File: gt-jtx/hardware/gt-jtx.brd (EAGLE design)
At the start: 100 x 80 mm, 8 parts, among them IC1 MEGA8-P

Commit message: Added ISCP pads on board for ATmega8 programming. Increased Route width for better transfer of toner to PCB. Routes are now on bottom layer so no need to mirror image for printing
git-svn-id: https://gt-jtx.googlecode.com/svn/trunk@18 79910f2a-facc-22ab-b1ea-80da55196309
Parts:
- added R2: (no value), resistor:0204V
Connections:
- new net N$25: IC1.1, R2.2
- net +5V: now also R2.1
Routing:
- net +5V: track 136.9 -> 153.7 mm, vias 0 -> 1
- net N$25: track 0.00 -> 6.35 mm, vias 0 -> 1
- net N$14: vias 0 -> 1
- net N$13: vias 0 -> 1
- net N$12: vias 0 -> 1
- net GND: vias 0 -> 1

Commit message: changed layer to use top layer.
git-svn-id: https://gt-jtx.googlecode.com/svn/trunk@19 79910f2a-facc-22ab-b1ea-80da55196309
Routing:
- net N$6: vias 0 -> 1

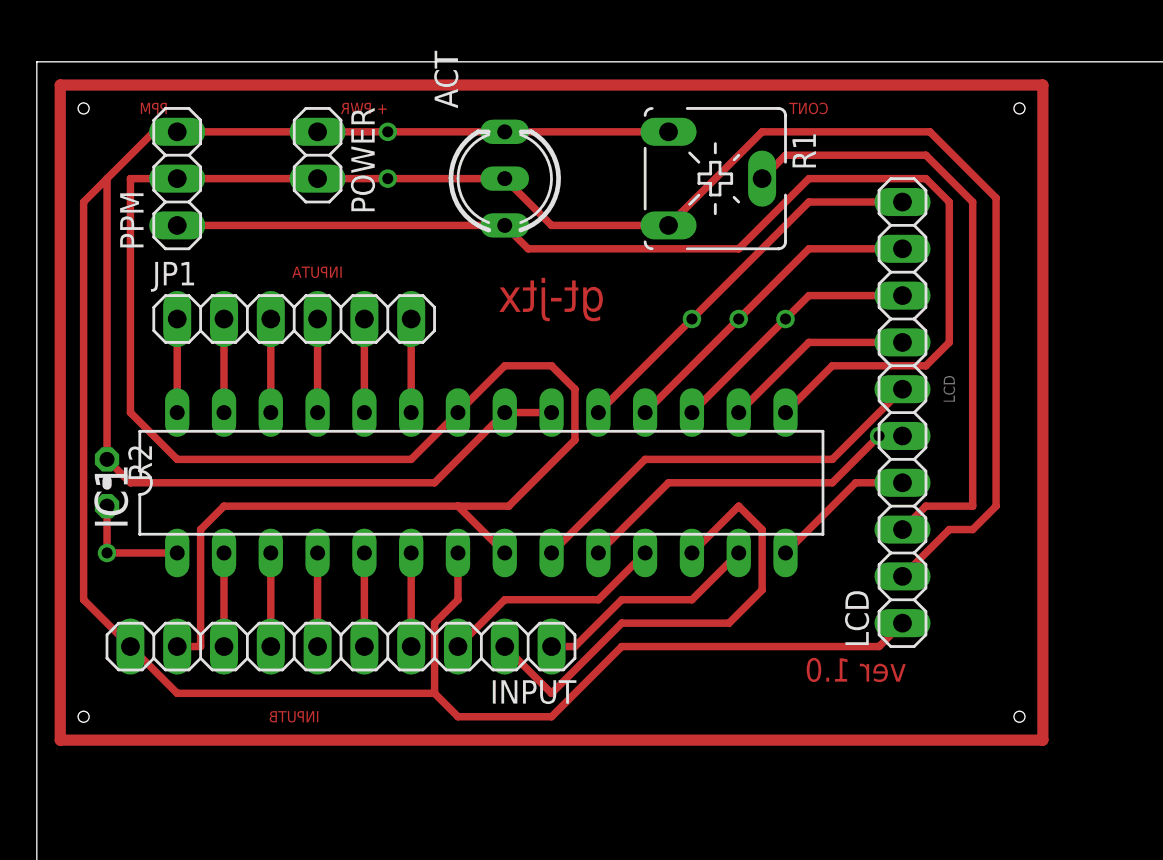
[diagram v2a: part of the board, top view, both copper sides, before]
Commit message: increased track width wherever possible to reduces chance of undercutting while etching. added necking in some areas of pcb
git-svn-id: https://gt-jtx.googlecode.com/svn/trunk@22 79910f2a-facc-22ab-b1ea-80da55196309
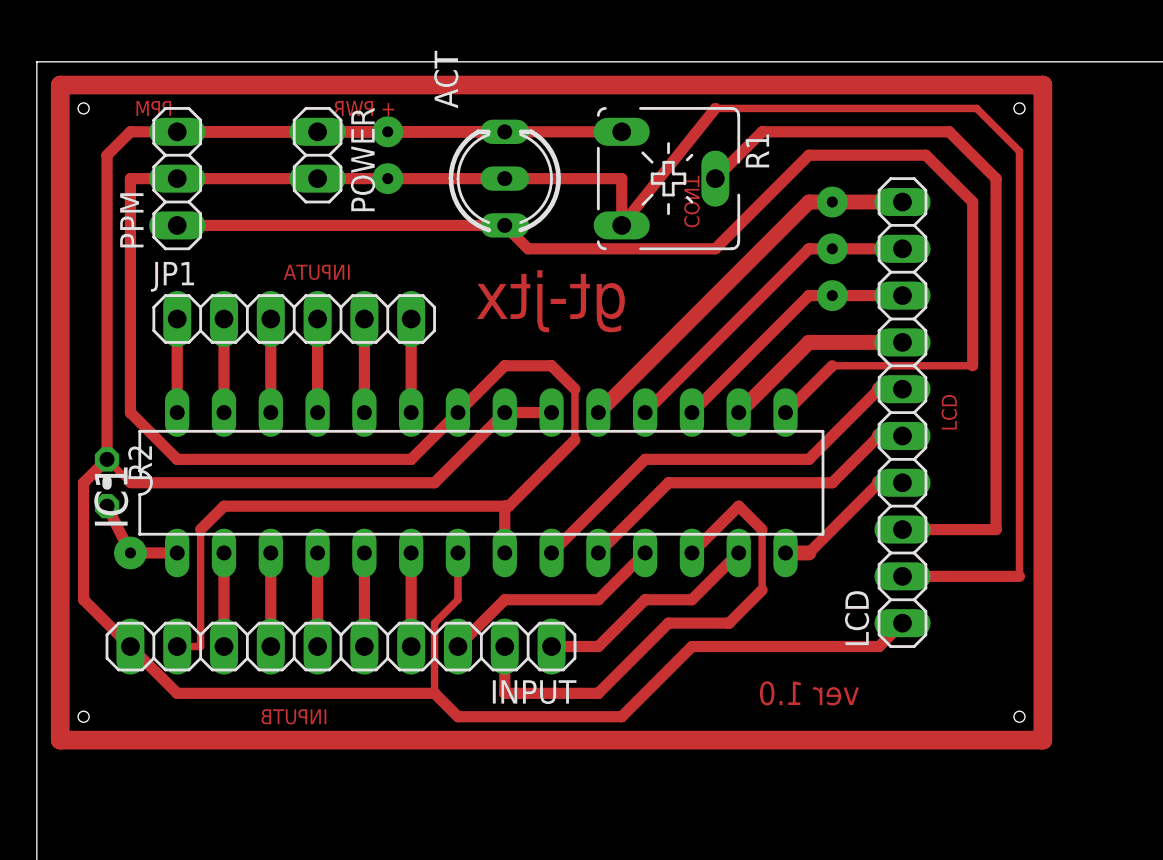
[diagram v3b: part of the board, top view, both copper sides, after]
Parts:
- moved R1 2.54 mm to (34.3, 73.7)
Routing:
- net GND: track 151.8 -> 160.0 mm
- net N$9: track 33.9 -> 41.5 mm
- net N$16: track 62.6 -> 67.0 mm
- net N$23: track 26.0 -> 27.5 mm
- net N$25: track 6.35 -> 5.38 mm
- net +5V: track 153.7 -> 154.5 mm
- net N$6: vias 1 -> 0
